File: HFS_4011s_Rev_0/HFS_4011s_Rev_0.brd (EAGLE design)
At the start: 47 x 44.5 mm, 57 parts, among them IC1 CP2104, J1 2X06, J2 2X12, J3 1X02, J5 1X02, Q1 mmbt2222, Q2 mmbt2222, Q3 MMUN2133LT1G, SW2 KMR2, U1 TPS61090RSAR, U2 MCP73831T-2ACI/OT, U3 AD5693R, U4 LM3671MF-3.3/NOPB, X2 ESP32_WROOM32_SKINNY

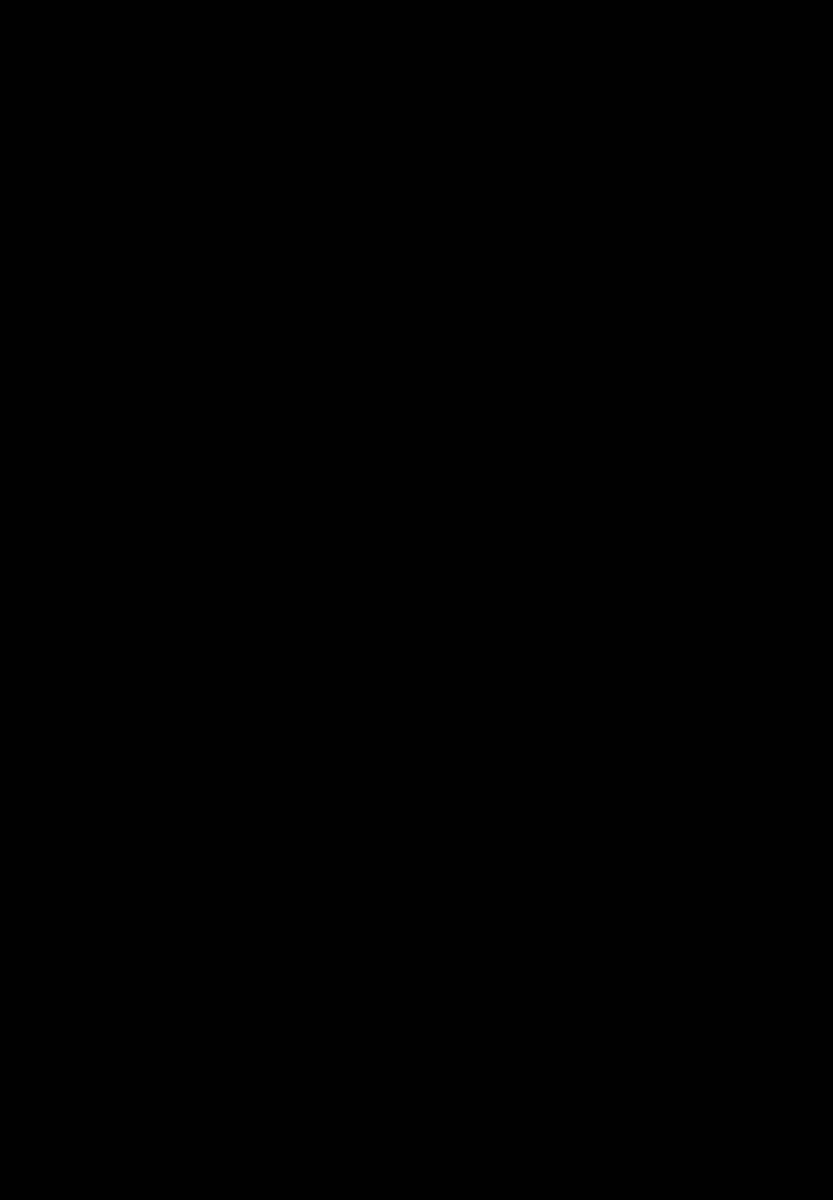
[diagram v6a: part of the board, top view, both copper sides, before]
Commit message: Working on IO. Need to get bigger connector for IO!
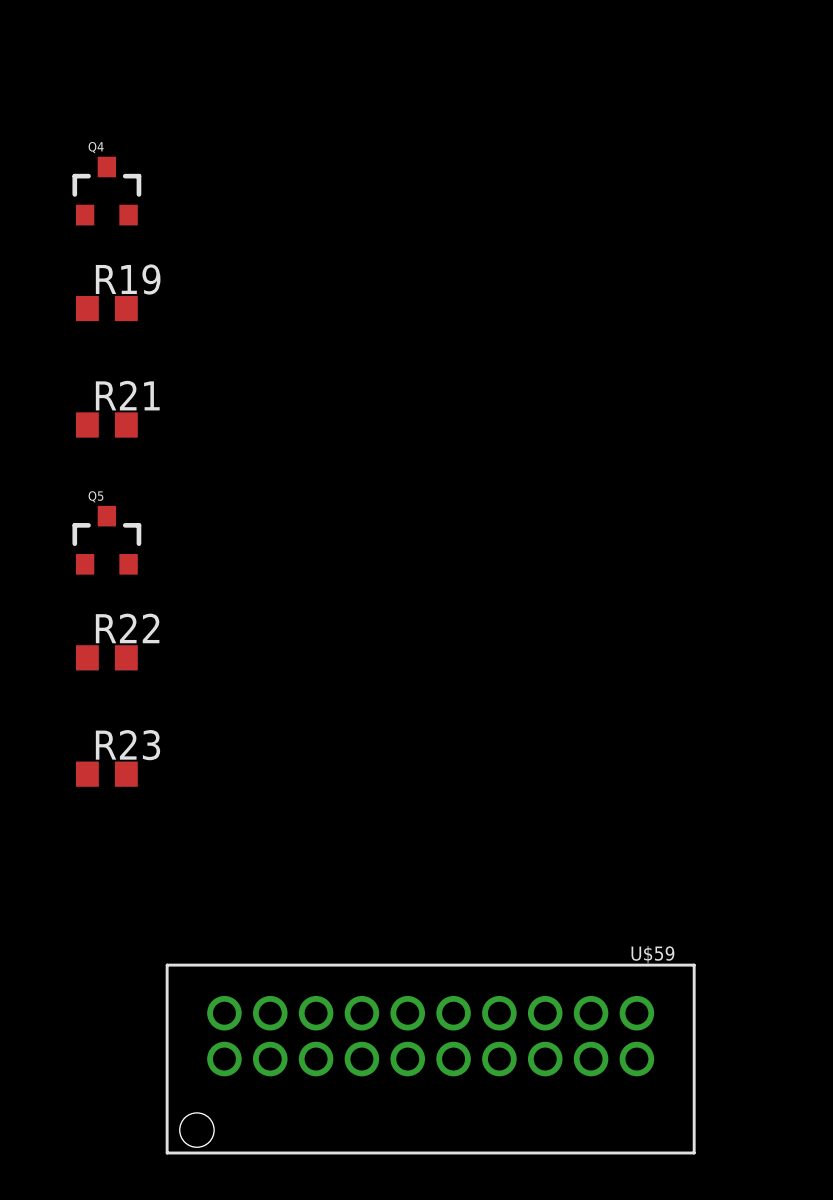
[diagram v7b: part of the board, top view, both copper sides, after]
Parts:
- added Q4, Q5: BSS138, SparkFun:SOT23-3
- added R19, R21, R22, R23: 5.1k, rcl:R0603
- added U$59: (no value), HFS4011sCustom:MOLEX_IGRID10X2CONNECTOR
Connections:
- new net LED_GND: U$59.P$2
- new net LED_VCC: U$59.P$1
- new net MIC1_AUD: U$59.P$7
- new net MIC1_GND: U$59.P$6
- new net MIC1_VCC: U$59.P$5
- new net MIC2_AUD: U$59.P$10
- new net MIC2_GND: U$59.P$9
- new net MIC2_VCC: U$59.P$8
- new net MOSI_5V: Q5.3, R23.1, U$59.P$4
- new net N$38: U$59.P$15
- new net N$42: U$59.P$16
- new net N$43: U$59.P$17
- new net N$44: U$59.P$18
- new net N$45: U$59.P$19
- new net N$46: U$59.P$20
- new net PB1_H: U$59.P$11
- new net PB1_L: U$59.P$12
- new net PB2_H: U$59.P$13
- new net PB2_L: U$59.P$14
- new net SCK_5V: Q4.3, R21.1, U$59.P$3
- net 3.3V: now also Q4.1, Q5.1, R19.2, R22.2
- net 5.0V: now also R21.2, R23.2
- net MOSI: now also Q5.2, R22.1
- net SCK: now also Q4.2, R19.1
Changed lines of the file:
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@@
 <element name="R16" library="rcl" library_urn="urn:adsk.eagle:library:334" package="R0603" package3d_urn="urn:adsk.eagle:package:23555/2" value="5.1k" x="-15.24" y="-234.95"/>
 <element name="J5" library="HFS4011sCustom" package="1X02" value="1X02" x="-8.89" y="-245.11"/>
+<element name="Q4" library="SparkFun" package="SOT23-3" value="BSS138" x="-15.24" y="-256.54"/>
+<element name="R19" library="rcl" library_urn="urn:adsk.eagle:library:334" package="R0603" package3d_urn="urn:adsk.eagle:package:23555/2" value="5.1k" x="-15.24" y="-261.62"/>
+<element name="R21" library="rcl" library_urn="urn:adsk.eagle:library:334" package="R0603" package3d_urn="urn:adsk.eagle:package:23555/2" value="5.1k" x="-15.24" y="-266.7"/>
+<element name="Q5" library="SparkFun" package="SOT23-3" value="BSS138" x="-15.24" y="-271.78"/>
+<element name="R22" library="rcl" library_urn="urn:adsk.eagle:library:334" package="R0603" package3d_urn="urn:adsk.eagle:package:23555/2" value="5.1k" x="-15.24" y="-276.86"/>
+<element name="R23" library="rcl" library_urn="urn:adsk.eagle:library:334" package="R0603" package3d_urn="urn:adsk.eagle:package:23555/2" value="5.1k" x="-15.24" y="-281.94"/>
+<element name="U$59" library="HFS4011sCustom" package="MOLEX_IGRID10X2CONNECTOR" value="" x="8.89" y="-293.37"/>
 </elements>
 <signals>
@@
 <contactref element="R17" pad="2"/>
 <contactref element="R18" pad="2"/>
+<contactref element="Q4" pad="1"/>
+<contactref element="R19" pad="2"/>
+<contactref element="Q5" pad="1"/>
+<contactref element="R22" pad="2"/>
 <wire x1="-14.39" y1="-219.71" x2="-14.39" y2="-224.79" width="0" layer="19" extent="1-1"/>
 <wire x1="-12.57" y1="-213.36" x2="-14.39" y2="-219.71" width="0" layer="19" extent="1-1"/>
@@
 <wire x1="-5.625" y1="-161.29" x2="-0.95" y2="-167.64" width="0" layer="19" extent="1-1"/>
 <wire x1="3.49" y1="-159.9899" x2="-0.95" y2="-167.64" width="0" layer="19" extent="1-1"/>
+<wire x1="-16.19" y1="-257.54" x2="-14.39" y2="-224.79" width="0" layer="19" extent="1-1"/>
+<wire x1="-14.39" y1="-261.62" x2="-16.19" y2="-257.54" width="0" layer="19" extent="1-1"/>
+<wire x1="-16.19" y1="-272.78" x2="-14.39" y2="-261.62" width="0" layer="19" extent="1-1"/>
+<wire x1="-14.39" y1="-276.86" x2="-16.19" y2="-272.78" width="0" layer="19" extent="1-1"/>
 <wire x1="8.02" y1="6.77" x2="3.49" y2="-159.9899" width="0" layer="19" extent="1-1"/>
 <wire x1="9.21" y1="25.4" x2="8.02" y2="6.77" width="0" layer="19" extent="1-1"/>
@@
 <signal name="MOSI">
 <contactref element="X2" pad="30"/>
+<contactref element="Q5" pad="2"/>
+<contactref element="R22" pad="1"/>
+<wire x1="-14.29" y1="-272.78" x2="31.36" y2="18.97" width="0" layer="19" extent="1-1"/>
+<wire x1="-16.09" y1="-276.86" x2="-14.29" y2="-272.78" width="0" layer="19" extent="1-1"/>
 </signal>
 <signal name="A5_IO4">
@@
 <signal name="SCK">
 <contactref element="X2" pad="29"/>
+<contactref element="Q4" pad="2"/>
+<contactref element="R19" pad="1"/>
+<wire x1="-14.29" y1="-257.54" x2="31.36" y2="17.7" width="0" layer="19" extent="1-1"/>
+<wire x1="-16.09" y1="-261.62" x2="-14.29" y2="-257.54" width="0" layer="19" extent="1-1"/>
 </signal>
 <signal name="A4_IO36">
@@
 <contactref element="C7" pad="+"/>
 <contactref element="J5" pad="1"/>
+<contactref element="R21" pad="2"/>
+<contactref element="R23" pad="2"/>
 <wire x1="14.29" y1="-104.14" x2="3.49" y2="-99.06" width="0" layer="19" extent="1-1"/>
 <wire x1="13.14" y1="-85.385" x2="3.49" y2="-99.06" width="0" layer="19" extent="1-1"/>
@@
 <wire x1="33.02" y1="-105.19" x2="14.29" y2="-104.14" width="0" layer="19" extent="1-1"/>
 <wire x1="-10.16" y1="-245.11" x2="14.29" y2="-104.14" width="0" layer="19" extent="1-1"/>
+<wire x1="-14.39" y1="-266.7" x2="-10.16" y2="-245.11" width="0" layer="19" extent="1-1"/>
+<wire x1="-14.39" y1="-281.94" x2="-14.39" y2="-266.7" width="0" layer="19" extent="1-1"/>
 </signal>
 <signal name="N$10">
@@
 <contactref element="J2" pad="23"/>
 </signal>
+<signal name="SCK_5V">
+<contactref element="Q4" pad="3"/>
+<contactref element="R21" pad="1"/>
+<contactref element="U$59" pad="P$3"/>
+<wire x1="-16.09" y1="-266.7" x2="-8.11" y2="-292.37" width="0" layer="19" extent="1-1"/>
+<wire x1="-15.24" y1="-255.44" x2="-16.09" y2="-266.7" width="0" layer="19" extent="1-1"/>
+</signal>
+<signal name="MOSI_5V">
+<contactref element="Q5" pad="3"/>
+<contactref element="R23" pad="1"/>
+<contactref element="U$59" pad="P$4"/>
+<wire x1="-16.09" y1="-281.94" x2="-8.11" y2="-294.37" width="0" layer="19" extent="1-1"/>
+<wire x1="-15.24" y1="-270.68" x2="-16.09" y2="-281.94" width="0" layer="19" extent="1-1"/>
+</signal>
+<signal name="LED_VCC">
+<contactref element="U$59" pad="P$1"/>
+</signal>
+<signal name="LED_GND">
+<contactref element="U$59" pad="P$2"/>
+</signal>
+<signal name="MIC1_VCC">
+<contactref element="U$59" pad="P$5"/>
+</signal>
+<signal name="MIC1_GND">
+<contactref element="U$59" pad="P$6"/>
+</signal>
+<signal name="MIC1_AUD">
+<contactref element="U$59" pad="P$7"/>
+</signal>
+<signal name="MIC2_VCC">
+<contactref element="U$59" pad="P$8"/>
+</signal>
+<signal name="MIC2_GND">
+<contactref element="U$59" pad="P$9"/>
+</signal>
+<signal name="MIC2_AUD">
+<contactref element="U$59" pad="P$10"/>
+</signal>
+<signal name="PB1_H">
+<contactref element="U$59" pad="P$11"/>
+</signal>
+<signal name="PB1_L">
+<contactref element="U$59" pad="P$12"/>
+</signal>
+<signal name="PB2_H">
+<contactref element="U$59" pad="P$13"/>
+</signal>
+<signal name="PB2_L">
+<contactref element="U$59" pad="P$14"/>
+</signal>
+<signal name="N$38">
+<contactref element="U$59" pad="P$15"/>
+</signal>
+<signal name="N$42">
+<contactref element="U$59" pad="P$16"/>
+</signal>
+<signal name="N$43">
+<contactref element="U$59" pad="P$17"/>
+</signal>
+<signal name="N$44">
+<contactref element="U$59" pad="P$18"/>
+</signal>
+<signal name="N$45">
+<contactref element="U$59" pad="P$19"/>
+</signal>
+<signal name="N$46">
+<contactref element="U$59" pad="P$20"/>
+</signal>
 </signals>

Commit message: Addded peripherals. Still need to connect IO from microcontroller to connector.
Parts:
- removed U$59: (no value), HFS4011sCustom:MOLEX_IGRID10X2CONNECTOR
- added J6: MOLEX_IGRID_15X2CONNECTOR, HFS4011sCustom:MOLEX_IGRID15X2CONNECTOR
- moved J5 249.9 mm to (33.0, 1.27), turned to 180 degrees
- moved J4 182.1 mm to (21.6, 6.35)
- moved J3 144.5 mm to (40.6, 26.7), turned to 90 degrees
- moved B1 128.2 mm to (40.6, 35.6), turned to 270 degrees
- moved IC1 26.2 mm to (14.0, 5.08)
- moved Q2 11.4 mm to (36.8, 17.8)
- moved J2 4.02 mm to (29.2, 44.5)
- moved J1 1.80 mm to (41.9, 7.62)
- moved X2 0.90 mm to (22.2, 23.5)
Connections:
- removed net LED_GND: U$59.P$2
- removed net LED_VCC: U$59.P$1
- removed net MIC1_GND: U$59.P$6
- removed net MIC1_VCC: U$59.P$5
- removed net MIC2_GND: U$59.P$9
- removed net MIC2_VCC: U$59.P$8
- removed net N$38: U$59.P$15
- removed net N$42: U$59.P$16
- removed net N$43: U$59.P$17
- removed net N$44: U$59.P$18
- removed net N$45: U$59.P$19
- removed net N$46: U$59.P$20
- new net SPKR_L_N: J6.P$18
- new net SPKR_L_P: J6.P$17
- new net SPKR_R_N: J6.P$22
- new net SPKR_R_P: J6.P$21
- net 3.3V: now also J6.P$27, J6.P$29, J6.P$5, J6.P$8
- net 5.0V: now also J6.P$1, J6.P$15, J6.P$19, J6.P$23, J6.P$25
- net GND: now also J6.P$16, J6.P$2, J6.P$20, J6.P$24, J6.P$26, J6.P$28, J6.P$30, J6.P$6, J6.P$9
- net MIC1_AUD: now also J6.P$7; no longer U$59.P$7
- net MIC2_AUD: now also J6.P$10; no longer U$59.P$10
- net MOSI_5V: now also J6.P$4; no longer U$59.P$4
- net PB1_H: now also J6.P$11; no longer U$59.P$11
- net PB1_L: now also J6.P$12; no longer U$59.P$12
- net PB2_H: now also J6.P$13; no longer U$59.P$13
- net PB2_L: now also J6.P$14; no longer U$59.P$14
- net SCK_5V: now also J6.P$3; no longer U$59.P$3
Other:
- board size 47 x 44.5 mm -> 44.5 x 47 mm
